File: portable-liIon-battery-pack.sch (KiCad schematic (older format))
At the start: 1 part

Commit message: beginings of TI design
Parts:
- added C? (x16): 0u1F, symbol C_Small
- added C?: 100pF, symbol C_Small
- added D? (x4): Green, symbol Led_Small
- added P?: BATT-SENSE, symbol CONN_01X05
- added Q? (x5): NMOS_GSD_Body-Diode, symbol NMOS_GSD_Body-Diode
- added R? (x5): 100, symbol R_Small
- added R?: 0.005, symbol R_Small
- added R? (x2): 0, symbol R_Small
- added R? (x8): 1k, symbol R_Small
- added R? (x4): 330k, symbol R_Small
- added R? (x2): 5k1, symbol R_Small
- added R?: 20k, symbol R_Small
- added RT? (x4): 10k, symbol Thermistor-Small
- added U?: BQ2947, symbol BQ2947
- added U?: BQ40Z60R, Housings_DFN_QFN:QFN-32-1EP_5x5mm_Pitch0.5mm, symbol BQ40Z60R
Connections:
- net labels added: +3.3V, GNDPWR, GNDREF
- wire segments 0 -> 111

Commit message: starting MAXIM design
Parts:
- removed C? (x16): 0u1F, symbol C_Small
- removed C?: 100pF, symbol C_Small
- removed D? (x4): Green, symbol Led_Small
- removed P?: BATT-SENSE, symbol CONN_01X05
- removed Q? (x5): NMOS_GSD_Body-Diode, symbol NMOS_GSD_Body-Diode
- removed R? (x5): 100, symbol R_Small
- removed R?: 0.005, symbol R_Small
- removed R? (x2): 0, symbol R_Small
- removed R? (x8): 1k, symbol R_Small
- removed R? (x4): 330k, symbol R_Small
- removed R? (x2): 5k1, symbol R_Small
- removed R?: 20k, symbol R_Small
- removed RT? (x4): 10k, symbol Thermistor-Small
- removed U?: LP2951-33DRG4, symbol LP2951-33DRG4
- removed U?: BQ2947, symbol BQ2947
- removed U?: BQ40Z60R, Housings_DFN_QFN:QFN-32-1EP_5x5mm_Pitch0.5mm, symbol BQ40Z60R
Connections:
- net labels removed: +3.3V, GNDPWR, GNDREF
- wire segments 111 -> 0

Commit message: started second config
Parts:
- added U?: BQ2947, symbol BQ2947
- added U?: ISL94203, Housings_DFN_QFN:UQFN-48-1EP_6x6mm_Pitch0.4mm, symbol ISL94203
- added U?: DS2788, Housings_SSOP:TSSOP-14_4.4x5mm_Pitch0.65mm, symbol DS2788
- added U?: MAX6765, symbol MAX6765
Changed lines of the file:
@@
 LIBS:SW-Passives
 LIBS:SW-Dexerials
+LIBS:SW-Intersil
 LIBS:portable-liIon-battery-pack-cache
 EELAYER 25 0
@@
 Comment4 ""
 $EndDescr
+$Comp
+L BQ2947 U?
+U 1 1 583F482D
+P 2450 1850
+F 0 "U?" H 2450 1750 60  0000 C CNN
+F 1 "BQ2947" H 2450 1950 60  0000 C CNN
+F 2 "" H 2350 1650 60  0001 C CNN
+F 3 "http://www.ti.com/lit/ds/symlink/bq2947.pdf" H 2300 2600 60  0001 C CNN
+F 4 "0.00@0" H 2450 900 60  0001 C CNN "Pricing"
+F 5 "Overvoltage Protection for 2-Series to 4-Series Cell Li-Ion Batteries withExternal DelayCapacitor" H 1800 2700 60  0001 C CNN "Description"
+F 6 "Texas Instruments" H 2450 1000 60  0001 C CNN "Manufacturer"
+F 7 "WSON8" H 2450 800 60  0001 C CNN "Package ID"
+	1    2450 1850
+	1    0    0    -1
+$EndComp
+$Comp
+L ISL94203 U?
+U 1 1 583F7609
+P 4800 3750
+F 0 "U?" H 4700 3650 60  0000 C CNN
+F 1 "ISL94203" H 4750 3950 60  0000 C CNN
+F 2 "Housings_DFN_QFN:UQFN-48-1EP_6x6mm_Pitch0.4mm" H 4950 1800 60  0001 C CNN
+F 3 "http://www.intersil.com/content/dam/Intersil/documents/isl9/isl94203.pdf" H 4800 1950 60  0001 C CNN
+F 4 "0.00@0" H 4900 5700 60  0001 C CNN "Pricing"
+F 5 "3 to 8 Cell Li-ion Battery Pack Monitor" H 4850 5450 60  0001 C CNN "Description"
+F 6 "48 Ld TQFN" H 4850 5550 60  0001 C CNN "Package ID"
+F 7 "Intersil" H 4800 5350 60  0001 C CNN "Manufacturer"
+	1    4800 3750
+	1    0    0    -1
+$EndComp
+$Comp
+L DS2788 U?
+U 1 1 583F8C9D
+P 7350 2000
+F 0 "U?" H 7600 1650 60  0000 C CNN
+F 1 "DS2788" H 7050 2350 60  0000 C CNN
+F 2 "Housings_SSOP:TSSOP-14_4.4x5mm_Pitch0.65mm" H 7400 1100 60  0001 C CNN
+F 3 "" H 7350 2000 60  0001 C CNN
+F 4 "0.00@0" H 7400 1000 60  0001 C CNN "Pricing"
+F 5 "Maxim Integrated" H 7400 2800 60  0001 C CNN "Manufacturer"
+F 6 "Stand-Alone Fuel-Gauge IC with LED Display Drivers" H 7550 2900 60  0001 C CNN "Description"
+F 7 "TSSOP-14" H 7450 3000 60  0001 C CNN "Package ID"
+	1    7350 2000
+	1    0    0    -1
+$EndComp
+$Comp
+L MAX6765 U?
+U 1 1 583F8F58
+P 7800 3500
+F 0 "U?" H 7700 3500 60  0000 C CNN
+F 1 "MAX6765" H 7900 4100 60  0000 C CNN
+F 2 "" H 7700 3050 60  0001 C CNN
+F 3 "" H 7800 3150 60  0001 C CNN
+F 4 "0.00@0" H 7800 2950 60  0001 C CNN "Pricing"
+F 5 "Automotive Micropower Linear Regulators with Supervisor" H 7750 3050 60  0001 C CNN "Description"
+F 6 "Maxim Integrated" H 7650 3150 60  0001 C CNN "Manufacturer"
+F 7 "TDFN-6" H 7750 2850 60  0001 C CNN "Package ID"
+	1    7800 3500
+	1    0    0    -1
+$EndComp
 $EndSCHEMATC

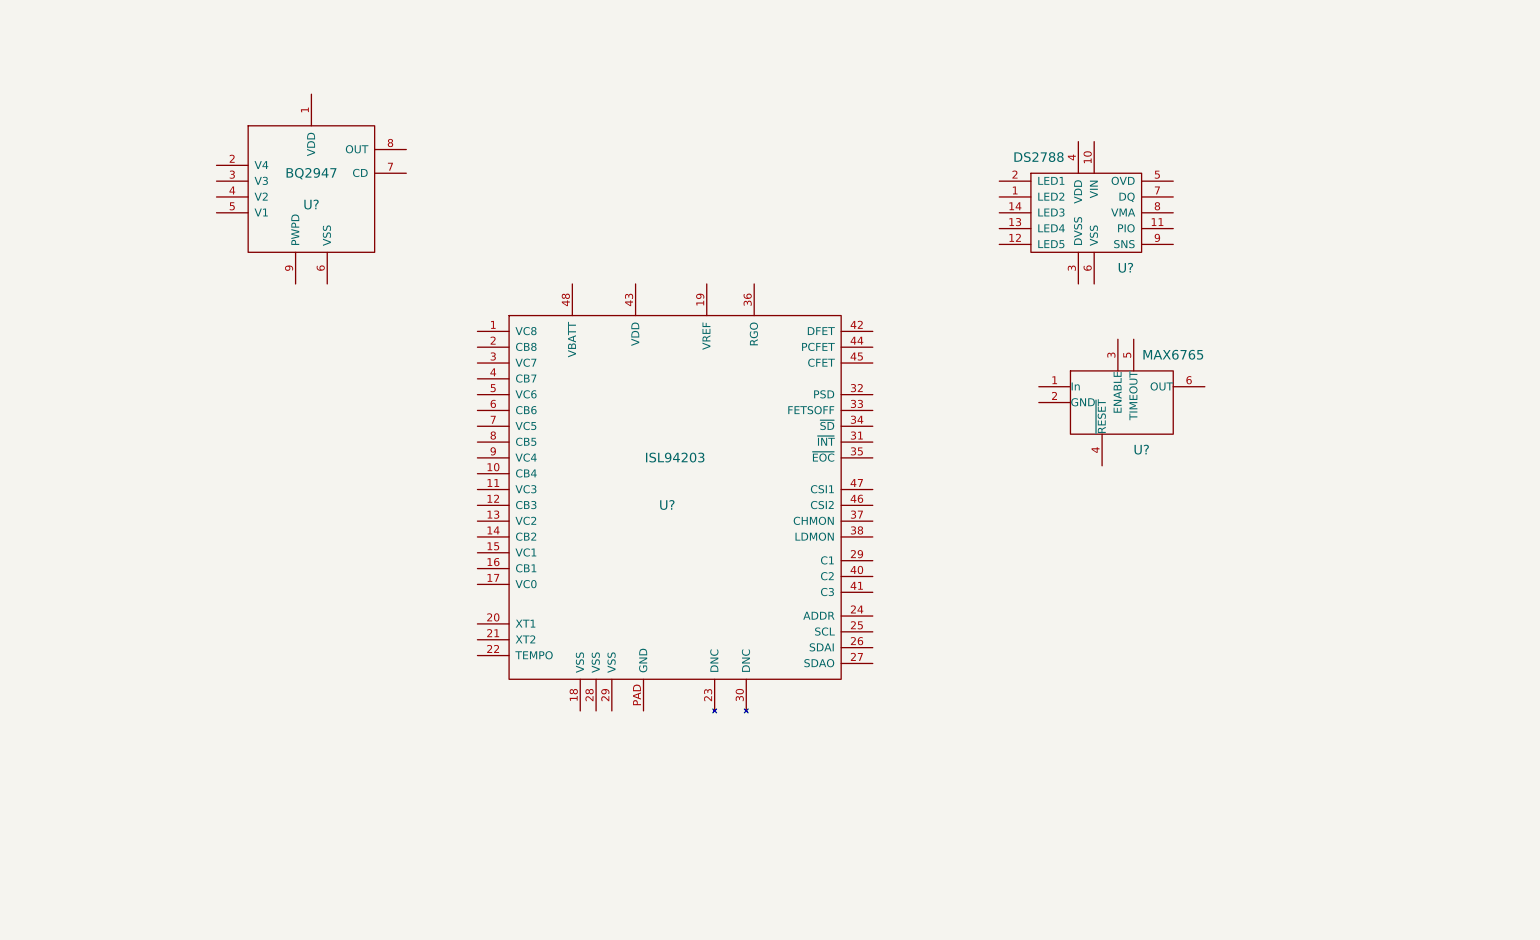
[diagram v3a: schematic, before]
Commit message: starting work on controller circuit and general orginization
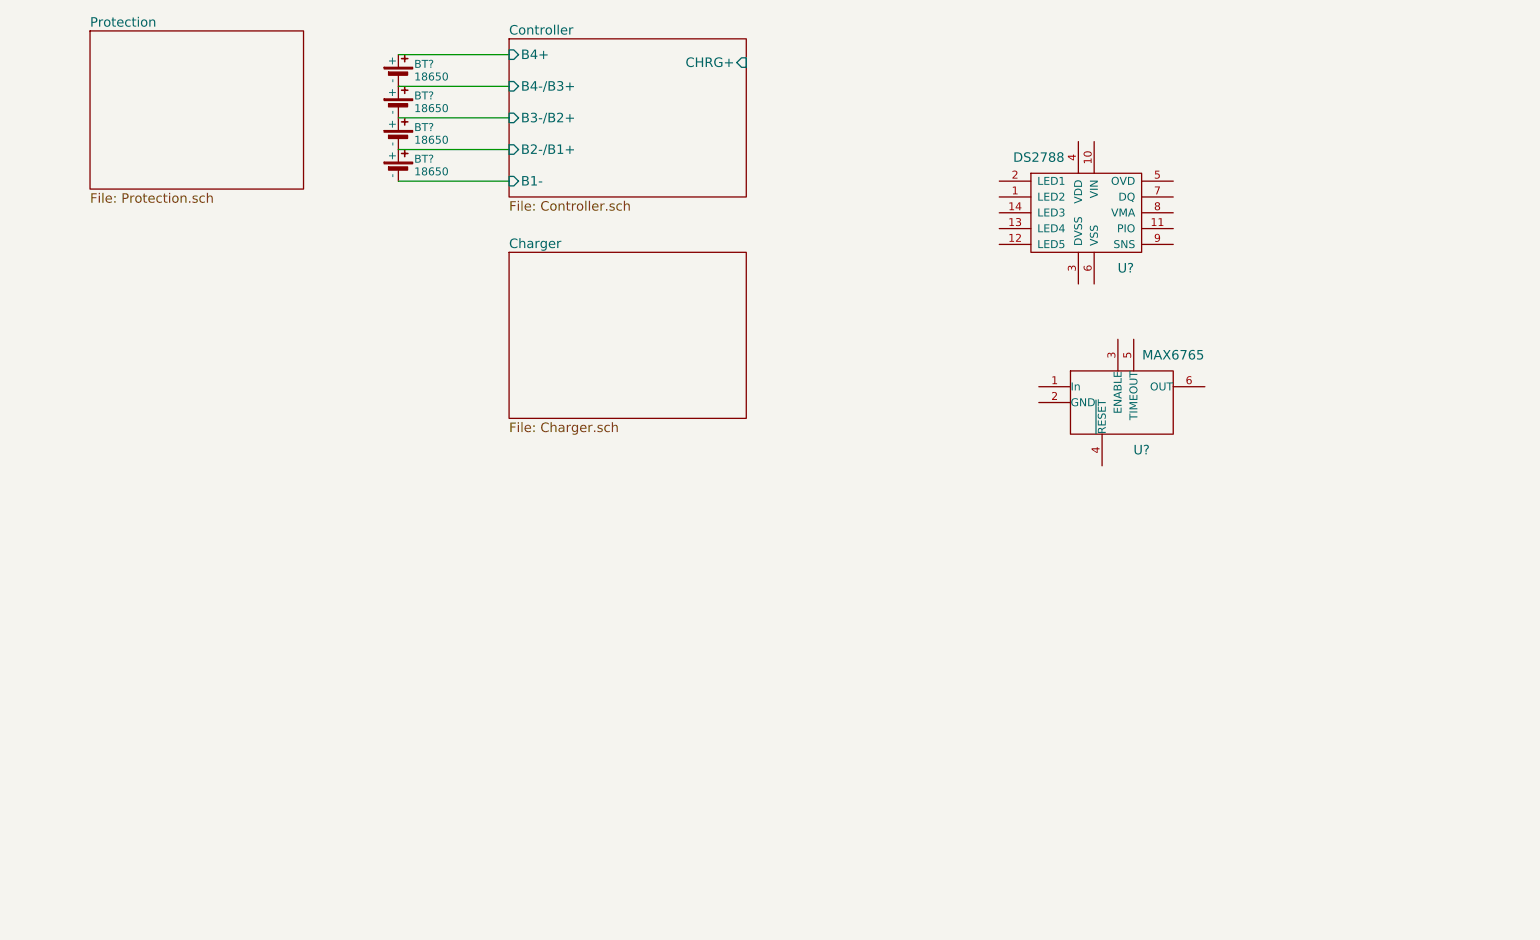
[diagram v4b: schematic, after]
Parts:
- removed U?: BQ2947, symbol BQ2947
- removed U?: ISL94203, Housings_DFN_QFN:UQFN-48-1EP_6x6mm_Pitch0.4mm, symbol ISL94203
- added BT? (x4): 18650, symbol 18650
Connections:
- new net Controller/B1-: BT?.2 (-)
- new net Controller/B2-/B1+: BT?.1 (+), BT?.2 (-)
- new net Controller/B3-/B2+: BT?.1 (+), BT?.2 (-)
- new net Controller/B4+: BT?.1 (+)
- new net Controller/B4-/B3+: BT?.1 (+), BT?.2 (-)
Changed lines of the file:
@@
 LIBS:SW-Dexerials
 LIBS:SW-Intersil
+LIBS:SW-Panasonic
 LIBS:portable-liIon-battery-pack-cache
 EELAYER 25 0
@@
 $Descr USLetter 11000 8500
 encoding utf-8
-Sheet 1 1
+Sheet 1 4
 Title ""
 Date ""
@@
 Comment4 ""
 $EndDescr
-$Comp
-L BQ2947 U?
-U 1 1 583F482D
-P 2450 1850
-F 0 "U?" H 2450 1750 60  0000 C CNN
-F 1 "BQ2947" H 2450 1950 60  0000 C CNN
-F 2 "" H 2350 1650 60  0001 C CNN
-F 3 "http://www.ti.com/lit/ds/symlink/bq2947.pdf" H 2300 2600 60  0001 C CNN
-F 4 "0.00@0" H 2450 900 60  0001 C CNN "Pricing"
-F 5 "Overvoltage Protection for 2-Series to 4-Series Cell Li-Ion Batteries withExternal DelayCapacitor" H 1800 2700 60  0001 C CNN "Description"
-F 6 "Texas Instruments" H 2450 1000 60  0001 C CNN "Manufacturer"
-F 7 "WSON8" H 2450 800 60  0001 C CNN "Package ID"
-	1    2450 1850
-	1    0    0    -1
-$EndComp
-$Comp
-L ISL94203 U?
-U 1 1 583F7609
-P 4800 3750
-F 0 "U?" H 4700 3650 60  0000 C CNN
-F 1 "ISL94203" H 4750 3950 60  0000 C CNN
-F 2 "Housings_DFN_QFN:UQFN-48-1EP_6x6mm_Pitch0.4mm" H 4950 1800 60  0001 C CNN
-F 3 "http://www.intersil.com/content/dam/Intersil/documents/isl9/isl94203.pdf" H 4800 1950 60  0001 C CNN
-F 4 "0.00@0" H 4900 5700 60  0001 C CNN "Pricing"
-F 5 "3 to 8 Cell Li-ion Battery Pack Monitor" H 4850 5450 60  0001 C CNN "Description"
-F 6 "48 Ld TQFN" H 4850 5550 60  0001 C CNN "Package ID"
-F 7 "Intersil" H 4800 5350 60  0001 C CNN "Manufacturer"
-	1    4800 3750
-	1    0    0    -1
-$EndComp
 $Comp
 L DS2788 U?
@@
 	1    0    0    -1
 $EndComp
+$Comp
+L 18650 BT?
+U 1 1 58A3E384
+P 3000 1100
+F 0 "BT?" H 3100 1140 50  0000 L CNN
+F 1 "18650" H 3100 1060 50  0000 L CNN
+F 2 "" V 3000 1110 50  0000 C CNN
+F 3 "" V 3000 1110 50  0000 C CNN
+F 4 "0.00@0" H 2975 1575 60  0001 C CNN "Pricing"
+F 5 "NCR 18650 cell battery" H 2975 1425 60  0001 C CNN "Description"
+F 6 "Panasonic" H 2975 1325 60  0001 C CNN "Manufacturer"
+	1    3000 1100
+	1    0    0    -1
+$EndComp
+$Comp
+L 18650 BT?
+U 1 1 58A3E3D7
+P 3000 1300
+F 0 "BT?" H 3100 1340 50  0000 L CNN
+F 1 "18650" H 3100 1260 50  0000 L CNN
+F 2 "" V 3000 1310 50  0000 C CNN
+F 3 "" V 3000 1310 50  0000 C CNN
+F 4 "0.00@0" H 2975 1775 60  0001 C CNN "Pricing"
+F 5 "NCR 18650 cell battery" H 2975 1625 60  0001 C CNN "Description"
+F 6 "Panasonic" H 2975 1525 60  0001 C CNN "Manufacturer"
+	1    3000 1300
+	1    0    0    -1
+$EndComp
+$Comp
+L 18650 BT?
+U 1 1 58A3E427
+P 3000 1500
+F 0 "BT?" H 3100 1540 50  0000 L CNN
+F 1 "18650" H 3100 1460 50  0000 L CNN
+F 2 "" V 3000 1510 50  0000 C CNN
+F 3 "" V 3000 1510 50  0000 C CNN
+F 4 "0.00@0" H 2975 1975 60  0001 C CNN "Pricing"
+F 5 "NCR 18650 cell battery" H 2975 1825 60  0001 C CNN "Description"
+F 6 "Panasonic" H 2975 1725 60  0001 C CNN "Manufacturer"
+	1    3000 1500
+	1    0    0    -1
+$EndComp
+$Comp
+L 18650 BT?
+U 1 1 58A3E468
+P 3000 1700
+F 0 "BT?" H 3100 1740 50  0000 L CNN
+F 1 "18650" H 3100 1660 50  0000 L CNN
+F 2 "" V 3000 1710 50  0000 C CNN
+F 3 "" V 3000 1710 50  0000 C CNN
+F 4 "0.00@0" H 2975 2175 60  0001 C CNN "Pricing"
+F 5 "NCR 18650 cell battery" H 2975 2025 60  0001 C CNN "Description"
+F 6 "Panasonic" H 2975 1925 60  0001 C CNN "Manufacturer"
+	1    3000 1700
+	1    0    0    -1
+$EndComp
+$Sheet
+S 3700 900  1500 1000
+U 58A64E5A
+F0 "Controller" 60
+F1 "Controller.sch" 60
+F2 "B4+" I L 3700 1000 60
+F3 "B4-/B3+" I L 3700 1200 60
+F4 "B3-/B2+" I L 3700 1400 60
+F5 "B2-/B1+" I L 3700 1600 60
+F6 "B1-" I L 3700 1800 60
+F7 "CHRG+" I R 5200 1050 60
+$EndSheet
+$Sheet
+S 3700 2250 1500 1050
+U 58A8E42A
+F0 "Charger" 60
+F1 "Charger.sch" 60
+$EndSheet
+Wire Wire Line
+	3000 1000 3700 1000
+Wire Wire Line
+	3000 1200 3700 1200
+Wire Wire Line
+	3000 1400 3700 1400
+Wire Wire Line
+	3000 1600 3700 1600
+Wire Wire Line
+	3000 1800 3700 1800
+$Sheet
+S 1050 850  1350 1000
+U 58A9B52D
+F0 "Protection" 60
+F1 "Protection.sch" 60
+$EndSheet
 $EndSCHEMATC

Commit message: These uncommitted files have been bugging me for waay tooo long
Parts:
- removed U?: DS2788, Housings_SSOP:TSSOP-14_4.4x5mm_Pitch0.65mm, symbol DS2788
- removed U?: MAX6765, symbol MAX6765
- gave numbers to parts that had none: 4
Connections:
- wire segments 5 -> 10
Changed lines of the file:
@@
 LIBS:SW-Fairchild-On-Semi
 LIBS:SW-ST
+LIBS:SW-Adafruit
 LIBS:portable-liIon-battery-pack-cache
 EELAYER 25 0
@@
 $Descr USLetter 11000 8500
 encoding utf-8
-Sheet 1 4
+Sheet 1 7
 Title ""
 Date ""
@@
 $EndDescr
 $Comp
-L DS2788 U?
-U 1 1 583F8C9D
-P 7350 2000
-F 0 "U?" H 7600 1650 60  0000 C CNN
-F 1 "DS2788" H 7050 2350 60  0000 C CNN
-F 2 "Housings_SSOP:TSSOP-14_4.4x5mm_Pitch0.65mm" H 7400 1100 60  0001 C CNN
-F 3 "" H 7350 2000 60  0001 C CNN
-F 4 "0.00@0" H 7400 1000 60  0001 C CNN "Pricing"
-F 5 "Maxim Integrated" H 7400 2800 60  0001 C CNN "Manufacturer"
-F 6 "Stand-Alone Fuel-Gauge IC with LED Display Drivers" H 7550 2900 60  0001 C CNN "Description"
-F 7 "TSSOP-14" H 7450 3000 60  0001 C CNN "Package ID"
-	1    7350 2000
-	1    0    0    -1
-$EndComp
-$Comp
-L MAX6765 U?
-U 1 1 583F8F58
-P 7800 3500
-F 0 "U?" H 7700 3500 60  0000 C CNN
-F 1 "MAX6765" H 7900 4100 60  0000 C CNN
-F 2 "" H 7700 3050 60  0001 C CNN
-F 3 "" H 7800 3150 60  0001 C CNN
-F 4 "0.00@0" H 7800 2950 60  0001 C CNN "Pricing"
-F 5 "Automotive Micropower Linear Regulators with Supervisor" H 7750 3050 60  0001 C CNN "Description"
-F 6 "Maxim Integrated" H 7650 3150 60  0001 C CNN "Manufacturer"
-F 7 "TDFN-6" H 7750 2850 60  0001 C CNN "Package ID"
-	1    7800 3500
-	1    0    0    -1
-$EndComp
-$Comp
-L 18650 BT?
+L 18650 BT1
 U 1 1 58A3E384
 P 3000 1100
-F 0 "BT?" H 3100 1140 50  0000 L CNN
+F 0 "BT1" H 3100 1140 50  0000 L CNN
 F 1 "18650" H 3100 1060 50  0000 L CNN
 F 2 "" V 3000 1110 50  0000 C CNN
@@
 $EndComp
 $Comp
-L 18650 BT?
+L 18650 BT2
 U 1 1 58A3E3D7
 P 3000 1300
-F 0 "BT?" H 3100 1340 50  0000 L CNN
+F 0 "BT2" H 3100 1340 50  0000 L CNN
 F 1 "18650" H 3100 1260 50  0000 L CNN
 F 2 "" V 3000 1310 50  0000 C CNN
@@
 $EndComp
 $Comp
-L 18650 BT?
+L 18650 BT3
 U 1 1 58A3E427
 P 3000 1500
-F 0 "BT?" H 3100 1540 50  0000 L CNN
+F 0 "BT3" H 3100 1540 50  0000 L CNN
 F 1 "18650" H 3100 1460 50  0000 L CNN
 F 2 "" V 3000 1510 50  0000 C CNN
@@
 $EndComp
 $Comp
-L 18650 BT?
+L 18650 BT4
 U 1 1 58A3E468
 P 3000 1700
-F 0 "BT?" H 3100 1740 50  0000 L CNN
+F 0 "BT4" H 3100 1740 50  0000 L CNN
 F 1 "18650" H 3100 1660 50  0000 L CNN
 F 2 "" V 3000 1710 50  0000 C CNN
@@
 $EndComp
 $Sheet
-S 3700 900  1500 1000
+S 3700 900  1500 1100
 U 58A64E5A
 F0 "Controller" 60
@@
 F5 "B2-/B1+" I L 3700 1600 60
 F6 "B1-" I L 3700 1800 60
-F7 "CHRG+" I R 5200 1050 60
+F7 "Charger+" I R 5200 950 60
+F8 "Load+" I R 5200 1050 60
+F9 "Charger/Load-" I R 5200 1150 60
+F10 "~EOC" I R 5200 1450 60
+F11 "~SD" I R 5200 1550 60
+F12 "RGO" I R 5200 1650 60
+F13 "FETSOFF" I R 5200 1750 60
+F14 "PSD" I R 5200 1850 60
+F15 "~INT" I R 5200 1950 60
+F16 "SDA" I R 5200 1250 60
+F17 "SCL" I R 5200 1350 60
 $EndSheet
 $Sheet
@@
 F0 "Charger" 60
 F1 "Charger.sch" 60
+F2 "Charge-Out" I R 5200 2600 60
+F3 "Charge-DCIN" I L 3700 2600 60
+F4 "~SHDN" I L 3700 2900 60
+F5 "ICTL" I L 3700 3050 60
+F6 "~ACOK" I L 3700 3200 60
 $EndSheet
 Wire Wire Line
-	3000 1000 3700 1000
+	9150 3550 9750 3550
+Wire Wire Line
+	2500 1000 3700 1000
+Wire Wire Line
+	9150 3750 9750 3750
 Wire Wire Line
 	3000 1200 3700 1200
 Wire Wire Line
+	9150 3950 9750 3950
+Wire Wire Line
 	3000 1400 3700 1400
+Wire Wire Line
+	9150 4150 9750 4150
 Wire Wire Line
 	3000 1600 3700 1600
 Wire Wire Line
-	3000 1800 3700 1800
+	9150 4350 9750 4350
+Wire Wire Line
+	2500 1800 3700 1800
 $Sheet
-S 1050 850  1350 1000
+S 7800 3450 1350 1000
 U 58A9B52D
 F0 "Protection" 60
 F1 "Protection.sch" 60
+F2 "B4+" I R 9150 4350 60
+F3 "B4-/B3+" I R 9150 4150 60
+F4 "B3-/B2+" I R 9150 3950 60
+F5 "B2-/B1+" I R 9150 3750 60
+F6 "B1-" I R 9150 3550 60
+F7 "OUT" I L 7800 3600 60
+$EndSheet
+$Sheet
+S 3700 3700 1500 1000
+U 58DC2ED5
+F0 "Microprocessor" 60
+F1 "microprocessor.sch" 60
+F2 "SDA" B L 3700 3900 60
+F3 "SCL" B L 3700 4050 60
+F4 "~CE" B L 3700 4200 60
+F5 "TXserial" B L 3700 4350 60
+$EndSheet
+Connection ~ 3000 1800
+Connection ~ 3000 1600
+Connection ~ 3000 1000
+Connection ~ 3000 1200
+Connection ~ 3000 1400
+$Sheet
+S 1300 850  1200 1100
+U 58DC77B6
+F0 "Battery Fuel Gauge" 60
+F1 "battery-fuel-gauge.sch" 60
+F2 "Pack+" I R 2500 1000 60
+F3 "Pack-" I R 2500 1800 60
+F4 "Data" I L 1300 1450 60
+$EndSheet
+$Sheet
+S 6650 1050 1800 1350
+U 58DD2FAD
+F0 "USBC Interface" 60
+F1 "USBC-PD.sch" 60
 $EndSheet
 $EndSCHEMATC
